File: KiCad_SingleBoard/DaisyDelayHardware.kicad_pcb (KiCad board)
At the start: 2 copper layers, 80.3 x 128.5 mm, 49 parts, among them J1 AUDIO_OUTPUT, J2 FEEDBACK_CV_INPUT, J3 DELAY_TIME_CV_INPUT, J5 AUDIO_INPUT, J6 Eurorack_Power_16pin_Shrouded, SW1 SW_SPDT, U1 LM4040DBZ-10, U2 TL074, U3 MCP6002-xP

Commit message: backup before pcb revision
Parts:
- C16: footprint Capacitor_THT:CP_Radial_D5.0mm_P2.50mm -> Capacitor_THT:CP_Radial_D8.0mm_P2.50mm
- J2: value FEEDBACK_CV_INPUT -> FBK_CV_IN
- J3: value DELAY_TIME_CV_INPUT -> D.TIME_CV_IN
- RV1: value DELAY_TIME_POT_10K -> DELAY_TIME_10K; footprint eurocad:Alpha9mmPot -> PCM_4ms_Potentiometer:Pot_9mm_DShaft
- RV2: value FEEDBACK_POT_10K -> FEEDBACK_10K; footprint eurocad:Alpha9mmPot -> PCM_4ms_Potentiometer:Pot_9mm_DShaft
- U1: value LM4040DBZ-10 -> LM4040
- moved C16 16.0 mm to (179.1, 70.7)
- moved RV2 0.38 mm to (177.8, 75.1), turned to 180 degrees
- moved RV1 0.38 mm to (177.8, 47.2), turned to 180 degrees
- moved R3 0.23 mm to (180.3, 40.2)
- renumbered SW1 to SWITCH
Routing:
- net Net-(C3-Pad2): track 11.3 -> 133.4 mm, vias 0 -> 1
- net ADC_IN_1: track 32.1 -> 151.5 mm
- net Net-(U2C--): track 0.00 -> 100.0 mm, vias 0 -> 2
- net Net-(U2B--): track 11.3 -> 97.5 mm, vias 0 -> 4
- net Net-(U3B--): track 96.0 -> 157.0 mm, vias 0 -> 4
- net GND: track 12.7 -> 65.5 mm, vias 0 -> 1
- net Net-(C4-Pad2): track 31.4 -> 83.8 mm, vias 0 -> 1
- net ADC_IN_0: track 39.9 -> 78.3 mm, vias 0 -> 1
- net +5V: track 77.1 -> 97.4 mm, vias 0 -> 1
- net Net-(C5-Pad2): track 27.2 -> 40.0 mm
- net Net-(U2D--): track 97.8 -> 107.4 mm, vias 0 -> 1
- net +12V: track 38.2 -> 44.1 mm
- net Net-(D1-A): track 42.4 -> 37.8 mm, vias 0 -> 2
- net SWITCH_IN: track 41.9 -> 46.0 mm
- net Net-(U3A--): track 192.9 -> 194.1 mm
- added copper zone on B.Cu, net GND
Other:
- board size 80.3 x 128.5 mm -> 29 x 106 mm
- board text removed: "AUDIO IN"
- board text removed: "AUDIO OUT"
- board text removed: "JLCJLCJLCJLC"
- board text removed: "LED"
- board text removed: "P1"
- board text removed: "P1 CV"
- board text removed: "P2"
- board text removed: "P2 CV"
- board text removed: "SEED FX"
- board text removed: "SWITCH"
- board text removed: "SynthLab"

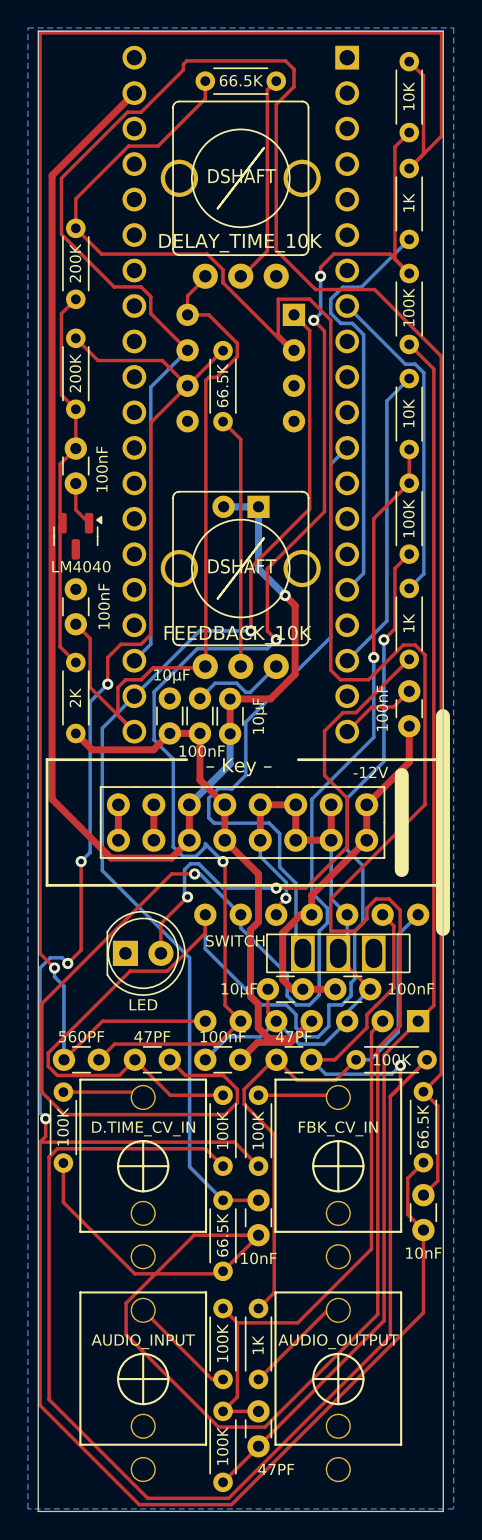
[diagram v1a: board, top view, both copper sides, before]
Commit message: pcb revised - but doesn't meet jlcpcb design rules
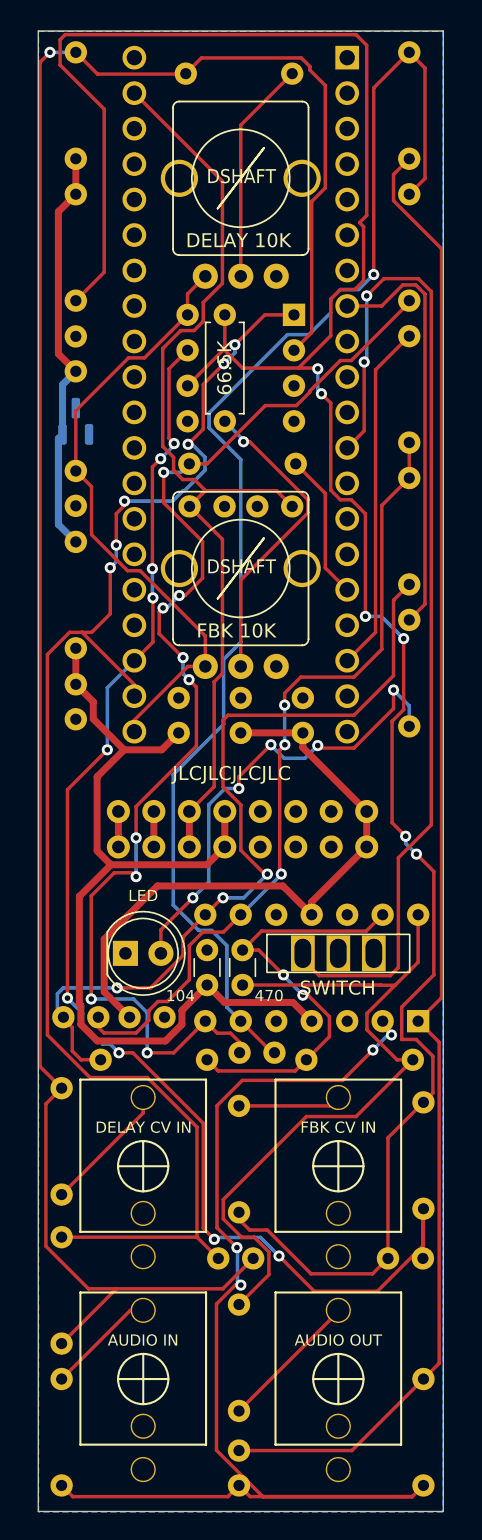
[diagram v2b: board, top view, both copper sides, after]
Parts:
- C1, C6: value 10nF -> 103; moved to B.Cu
- C10: value 100nF -> 104
- C11, C12, C15: value 10µF -> 103; moved to B.Cu
- C13, C14, C7, C8, C9: value 100nF -> 104; moved to B.Cu
- C16: value 220µF -> 104; footprint Capacitor_THT:CP_Radial_D8.0mm_P2.50mm -> Capacitor_THT:C_Disc_D3.0mm_W1.6mm_P2.50mm
- C2, C4: value 47PF -> 470; moved to B.Cu
- C3: value 560PF -> 561; moved to B.Cu
- C5: value 47PF -> 470
- J1: value AUDIO_OUTPUT -> AUDIO OUT
- J2: value FBK_CV_IN -> FBK CV IN
- J3: value D.TIME_CV_IN -> DELAY CV IN
- J5: value AUDIO_INPUT -> AUDIO IN
- J6, U1: moved to B.Cu
- R1, R10, R11, R12, R13, R14, R15, R16, R18, R19, R2, R20, R3, R4, R5, R6, R7, R8, R9: footprint Resistor_THT:R_Axial_DIN0204_L3.6mm_D1.6mm_P5.08mm_Horizontal -> Resistor_THT:R_Axial_DIN0207_L6.3mm_D2.5mm_P7.62mm_Horizontal; moved to B.Cu
- R17: footprint Resistor_THT:R_Axial_DIN0204_L3.6mm_D1.6mm_P5.08mm_Horizontal -> Resistor_THT:R_Axial_DIN0207_L6.3mm_D2.5mm_P7.62mm_Horizontal
- RV1: value DELAY_TIME_10K -> DELAY 10K
- RV2: value FEEDBACK_10K -> FBK 10K
- U3: value MCP6002-xP -> MCP6002
- moved R7 26.4 mm to (174.1, 67.6), turned to 0 degrees
- moved C11 18.9 mm to (177.8, 86.9), turned to 90 degrees
- moved C15 16.5 mm to (174.1, 70.7), turned to 0 degrees
- moved R15 15.4 mm to (166.0, 48.3), turned to -90 degrees
- moved R8 15.3 mm to (190.9, 140.8), turned to 90 degrees
- moved C9 14.9 mm to (172.3, 107.3)
- moved R6 13.3 mm to (189.9, 45.8)
- moved R4 12.7 mm to (165.0, 130.6)
- moved C3 12.6 mm to (180.2, 109.8)
- moved R5 11.6 mm to (165.0, 133.2), turned to -90 degrees
- moved C8 11.0 mm to (166.0, 68.1), turned to -90 degrees
- moved R1 10.1 mm to (166.0, 45.8)
- moved C5 9.27 mm to (177.9, 102.5), turned to -90 degrees
- moved R12 9.12 mm to (167.8, 110.3), turned to 0 degrees
- moved R13 8.64 mm to (182.5, 110.3), turned to 0 degrees
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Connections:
- net -10V_REF renamed -10V
- net 3V3_A renamed +3V3
- C15 pad 2: +5V -> GND
- C16 pad 2: +5V -> GND
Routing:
- net Net-(U2D--): track 107.4 -> 30.9 mm, vias 1 -> 2
- net GND: track 65.5 -> 0.00 mm, vias 1 -> 0
- net ADC_IN_1: track 151.5 -> 97.0 mm, vias 0 -> 9
- net Net-(C3-Pad2): track 133.4 -> 85.1 mm, vias 1 -> 9
- net Net-(U2A--): track 39.2 -> 84.8 mm, vias 0 -> 4
- net Net-(U3A--): track 194.1 -> 151.1 mm, vias 0 -> 1
- net Net-(U2C--): track 100.0 -> 57.6 mm, vias 2 -> 3
- net SWITCH_IN: track 46.0 -> 74.3 mm, vias 0 -> 2
- net +5V: track 97.4 -> 71.3 mm, vias 1 -> 0
- net ADC_IN_0: track 78.3 -> 103.6 mm, vias 1 -> 6
- net Net-(C4-Pad2): track 83.8 -> 59.2 mm, vias 1 -> 3
- net +12V: track 44.1 -> 66.5 mm
- net AUDIO_IN_L: track 30.1 -> 10.5 mm
- net -12V: track 26.4 -> 44.6 mm
- net Net-(C2-Pad2): track 88.5 -> 106.4 mm
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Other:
- board text added: "JLCJLCJLCJLC"

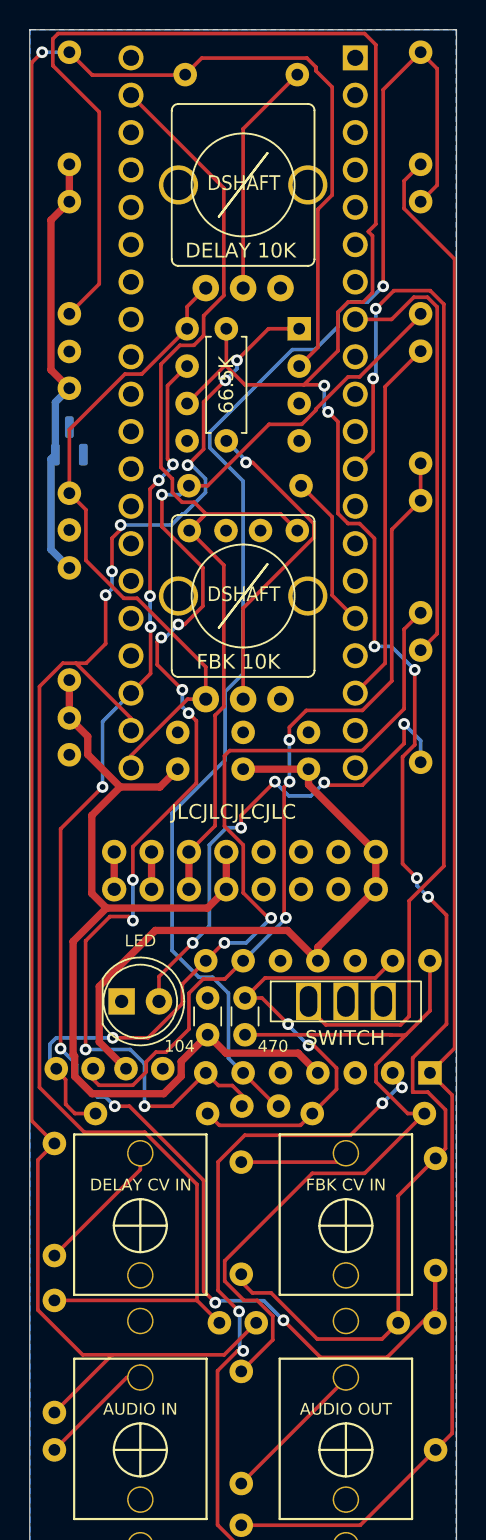
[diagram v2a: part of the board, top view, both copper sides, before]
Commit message: DRC now adheres to custom design rules for jlcpcb
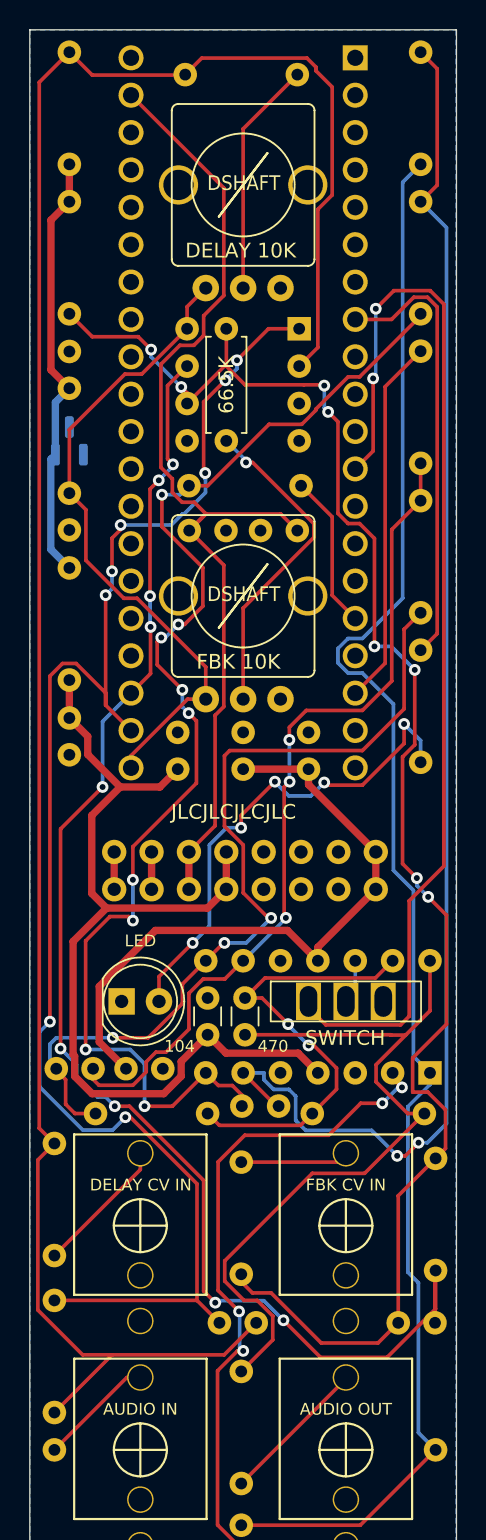
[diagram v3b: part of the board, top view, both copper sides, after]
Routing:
- net Net-(U3B--): track 168.7 -> 111.0 mm, vias 6 -> 8
- net Net-(C2-Pad2): track 106.4 -> 110.2 mm
- net GND: track 0.00 -> 3.03 mm
- net Net-(U3A--): track 151.1 -> 149.6 mm, vias 1 -> 0
- net ADC_IN_0: track 103.6 -> 104.8 mm, vias 6 -> 8
- net Net-(U2B--): track 96.9 -> 96.1 mm, vias 1 -> 2
